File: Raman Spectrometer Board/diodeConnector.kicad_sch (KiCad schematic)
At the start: 15 parts, among them J5 Conn_01x02, Q1 BSS138, Q2 AO3401A, Q3 AO3401A, Q4 BSS138

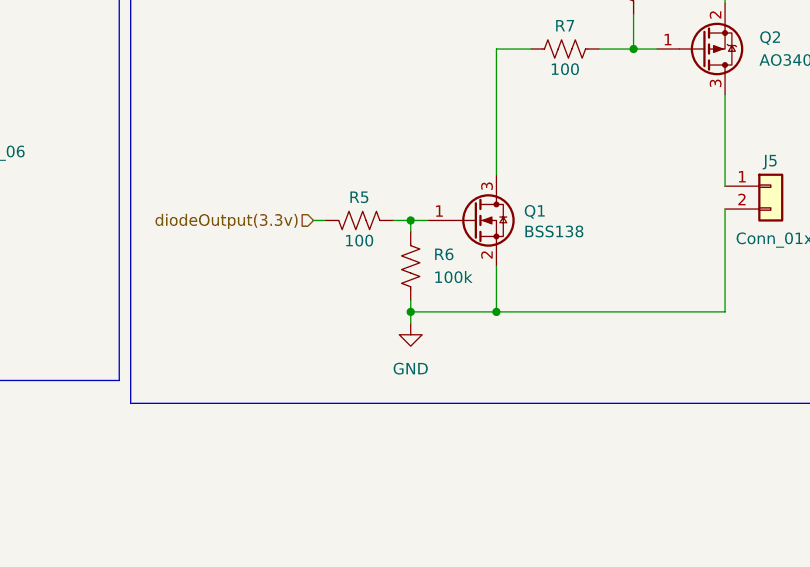
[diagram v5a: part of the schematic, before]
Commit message: Began re-laying out laser driver section
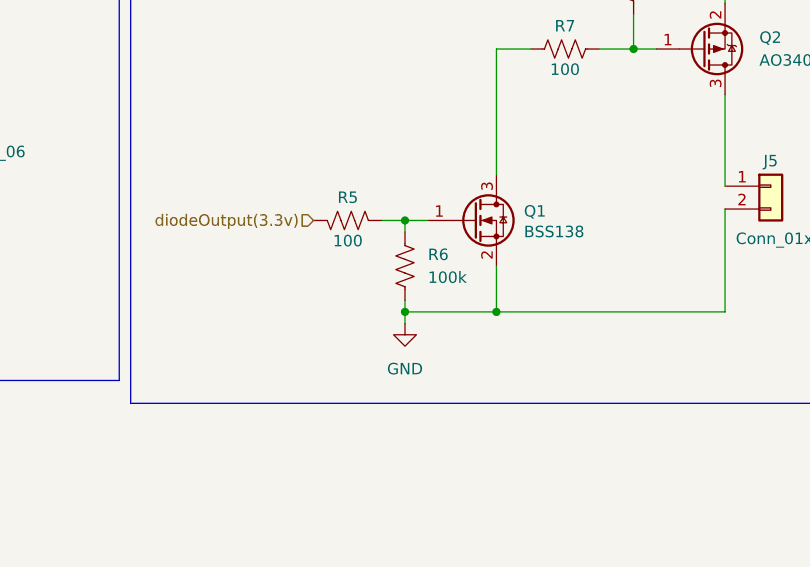
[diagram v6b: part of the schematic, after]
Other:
- moved on the sheet: R5, R6
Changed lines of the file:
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@@
 	)
 	(junction
-		(at 122.555 80.01)
+		(at 121.92 69.85)
 		(diameter 0)
 		(color 0 0 0 0)
@@
 	)
 	(junction
-		(at 236.22 34.29)
+		(at 121.92 80.01)
 		(diameter 0)
 		(color 0 0 0 0)
 	)
 	(junction
-		(at 122.555 69.85)
+		(at 236.22 34.29)
 		(diameter 0)
 		(color 0 0 0 0)
@@
 	(wire
 		(pts
+			(xy 121.92 69.85) (xy 119.38 69.85)
+		)
+		(stroke
+			(width 0)
+			(type default)
+		)
+	)
+	(wire
+		(pts
+			(xy 121.92 69.85) (xy 124.46 69.85)
+		)
+		(stroke
+			(width 0)
+			(type default)
+		)
+	)
+	(wire
+		(pts
 			(xy 252.73 73.66) (xy 261.62 73.66)
 		)
@@
 	(wire
 		(pts
-			(xy 122.555 78.74) (xy 122.555 80.01)
+			(xy 121.92 78.74) (xy 121.92 80.01)
 		)
 		(stroke
@@
 	(wire
 		(pts
-			(xy 122.555 80.01) (xy 132.08 80.01)
-		)
-		(stroke
-			(width 0)
-			(type default)
-		)
-	)
-	(wire
-		(pts
 			(xy 245.11 78.74) (xy 245.11 91.44)
 		)
@@
 	(wire
 		(pts
-			(xy 122.555 69.85) (xy 122.555 71.12)
-		)
-		(stroke
-			(width 0)
-			(type default)
-		)
-	)
-	(wire
-		(pts
-			(xy 124.46 69.85) (xy 122.555 69.85)
+			(xy 121.92 69.85) (xy 121.92 71.12)
 		)
 		(stroke
@@
 	(wire
 		(pts
+			(xy 121.92 80.01) (xy 132.08 80.01)
+		)
+		(stroke
+			(width 0)
+			(type default)
+		)
+	)
+	(wire
+		(pts
 			(xy 157.48 38.1) (xy 157.48 45.72)
 		)
@@
 	(wire
 		(pts
-			(xy 113.03 69.85) (xy 111.76 69.85)
-		)
-		(stroke
-			(width 0)
-			(type default)
-		)
-	)
-	(wire
-		(pts
 			(xy 157.48 36.83) (xy 157.48 38.1)
 		)
@@
 	(wire
 		(pts
-			(xy 122.555 80.01) (xy 122.555 81.28)
-		)
-		(stroke
-			(width 0)
-			(type default)
-		)
-	)
-	(wire
-		(pts
-			(xy 122.555 69.85) (xy 120.65 69.85)
+			(xy 121.92 80.01) (xy 121.92 81.28)
 		)
 		(stroke
@@
 		(dnp no)
 		(fields_autoplaced yes)
-		(property "Reference" "#PWR029"
+		(property "Reference" "#PWR032"
 			(at 228.6 97.79 0)
 			(effects
@@
 			(project "RamanSpectrometerBoard"
 				(path "/ab487c59-f066-48f5-a383-99e8eaf806bf/c790a08a-952a-47a5-8a2d-3628381b83e8"
-					(reference "#PWR029")
+					(reference "#PWR032")
 					(unit 1)
 				)
@@
 	(symbol
 		(lib_id "Device:R_US")
-		(at 122.555 74.93 180)
+		(at 121.92 74.93 180)
 		(unit 1)
 		(exclude_from_sim no)
@@
 		(dnp no)
 		(property "Reference" "R6"
-			(at 125.095 73.6599 0)
+			(at 124.46 73.6599 0)
 			(effects
 				(font
@@
 		)
 		(property "Value" "100k"
-			(at 125.095 76.1999 0)
+			(at 124.46 76.1999 0)
 			(effects
 				(font
@@
 		)
 		(property "Footprint" "Resistor_SMD:R_0603_1608Metric_Pad0.98x0.95mm_HandSolder"
-			(at 121.539 74.676 90)
+			(at 120.904 74.676 90)
 			(effects
 				(font
@@
 		)
 		(property "Datasheet" "~"
-			(at 122.555 74.93 0)
+			(at 121.92 74.93 0)
 			(effects
 				(font
@@
 		)
 		(property "Description" "Resistor, US symbol"
-			(at 122.555 74.93 0)
+			(at 121.92 74.93 0)
 			(effects
 				(font
@@
 		(dnp no)
 		(fields_autoplaced yes)
-		(property "Reference" "#PWR030"
+		(property "Reference" "#PWR033"
 			(at 236.22 35.56 0)
 			(effects
@@
 			(project ""
 				(path "/ab487c59-f066-48f5-a383-99e8eaf806bf/c790a08a-952a-47a5-8a2d-3628381b83e8"
-					(reference "#PWR030")
+					(reference "#PWR033")
 					(unit 1)
 				)
@@
 		(dnp no)
 		(fields_autoplaced yes)
-		(property "Reference" "#PWR023"
+		(property "Reference" "#PWR026"
 			(at 45.72 58.42 0)
 			(effects
@@
 			(project "RamanSpectrometerBoard"
 				(path "/ab487c59-f066-48f5-a383-99e8eaf806bf/c790a08a-952a-47a5-8a2d-3628381b83e8"
-					(reference "#PWR023")
+					(reference "#PWR026")
 					(unit 1)
 				)
@@
 		(dnp no)
 		(fields_autoplaced yes)
-		(property "Reference" "#PWR026"
+		(property "Reference" "#PWR029"
 			(at 58.42 153.67 0)
 			(effects
@@
 			(project "RamanSpectrometerBoard"
 				(path "/ab487c59-f066-48f5-a383-99e8eaf806bf/c790a08a-952a-47a5-8a2d-3628381b83e8"
-					(reference "#PWR026")
+					(reference "#PWR029")
 					(unit 1)
 				)
@@
 		(dnp no)
 		(fields_autoplaced yes)
-		(property "Reference" "#PWR025"
+		(property "Reference" "#PWR028"
 			(at 58.42 133.35 0)
 			(effects
@@
 			(project "RamanSpectrometerBoard"
 				(path "/ab487c59-f066-48f5-a383-99e8eaf806bf/c790a08a-952a-47a5-8a2d-3628381b83e8"
-					(reference "#PWR025")
+					(reference "#PWR028")
 					(unit 1)
 				)
@@
 	(symbol
 		(lib_id "Device:R_US")
-		(at 116.84 69.85 270)
+		(at 115.57 69.85 270)
 		(mirror x)
 		(unit 1)
@@
 		(dnp no)
 		(property "Reference" "R5"
-			(at 116.84 67.31 90)
+			(at 115.57 67.31 90)
 			(effects
 				(font
@@
 		)
 		(property "Value" "100"
-			(at 116.84 72.136 90)
+			(at 115.57 72.136 90)
 			(effects
 				(font
@@
 		)
 		(property "Footprint" "Resistor_SMD:R_0603_1608Metric_Pad0.98x0.95mm_HandSolder"
-			(at 116.586 68.834 90)
+			(at 115.316 68.834 90)
 			(effects
 				(font
@@
 		)
 		(property "Datasheet" "~"
-			(at 116.84 69.85 0)
+			(at 115.57 69.85 0)
 			(effects
 				(font
@@
 		)
 		(property "Description" "Resistor, US symbol"
-			(at 116.84 69.85 0)
+			(at 115.57 69.85 0)
 			(effects
 				(font
@@
 	(symbol
 		(lib_id "power:GND")
-		(at 122.555 81.28 0)
+		(at 121.92 81.28 0)
 		(mirror y)
 		(unit 1)
@@
 		(dnp no)
 		(fields_autoplaced yes)
-		(property "Reference" "#PWR027"
-			(at 122.555 87.63 0)
+		(property "Reference" "#PWR030"
+			(at 121.92 87.63 0)
 			(effects
 				(font
@@
 		)
 		(property "Value" "GND"
-			(at 122.555 86.36 0)
+			(at 121.92 86.36 0)
 			(effects
 				(font
@@
 		)
 		(property "Footprint" ""
-			(at 122.555 81.28 0)
+			(at 121.92 81.28 0)
 			(effects
 				(font
@@
 		)
 		(property "Datasheet" ""
-			(at 122.555 81.28 0)
+			(at 121.92 81.28 0)
 			(effects
 				(font
@@
 		)
 		(property "Description" "Power symbol creates a global label with name \"GND\" , ground"
-			(at 122.555 81.28 0)
+			(at 121.92 81.28 0)
 			(effects
 				(font
@@
 			(project "RamanSpectrometerBoard"
 				(path "/ab487c59-f066-48f5-a383-99e8eaf806bf/c790a08a-952a-47a5-8a2d-3628381b83e8"
-					(reference "#PWR027")
+					(reference "#PWR030")
 					(unit 1)
 				)
@@
 		(dnp no)
 		(fields_autoplaced yes)
-		(property "Reference" "#PWR024"
+		(property "Reference" "#PWR027"
 			(at 57.15 78.74 0)
 			(effects
@@
 			(project "RamanSpectrometerBoard"
 				(path "/ab487c59-f066-48f5-a383-99e8eaf806bf/c790a08a-952a-47a5-8a2d-3628381b83e8"
-					(reference "#PWR024")
+					(reference "#PWR027")
 					(unit 1)
 				)
@@
 		(dnp no)
 		(fields_autoplaced yes)
-		(property "Reference" "#PWR028"
+		(property "Reference" "#PWR031"
 			(at 157.48 40.64 0)
 			(effects
@@
 			(project ""
 				(path "/ab487c59-f066-48f5-a383-99e8eaf806bf/c790a08a-952a-47a5-8a2d-3628381b83e8"
-					(reference "#PWR028")
-					(unit 1)
-				)
+					(reference "#PWR031")
+					(unit 1)
+				)

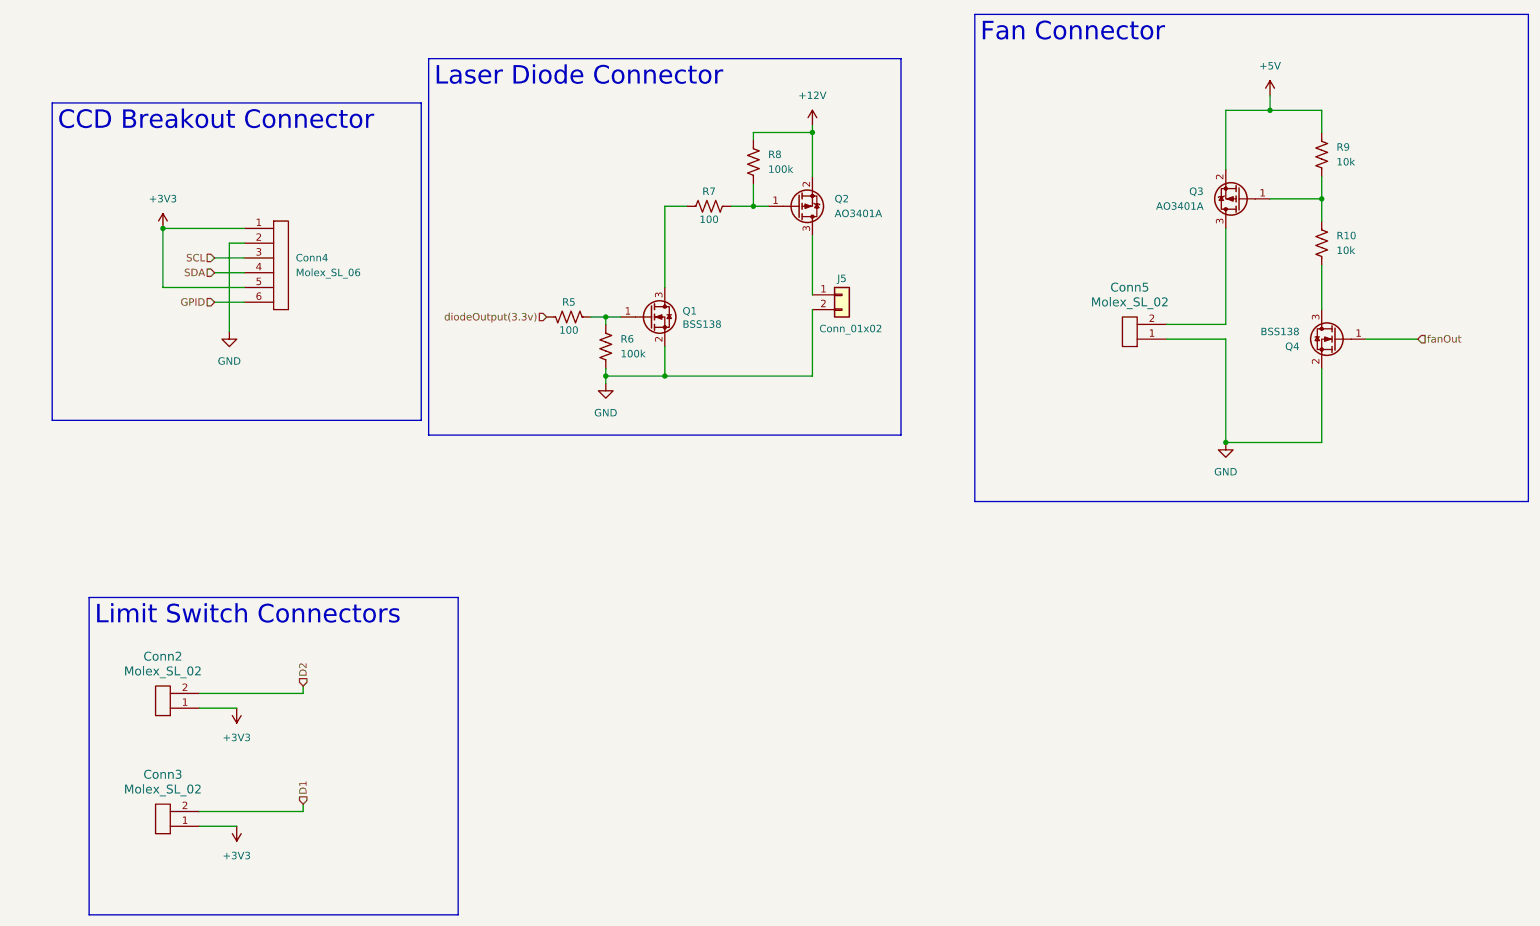
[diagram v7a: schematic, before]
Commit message: SCH fixes
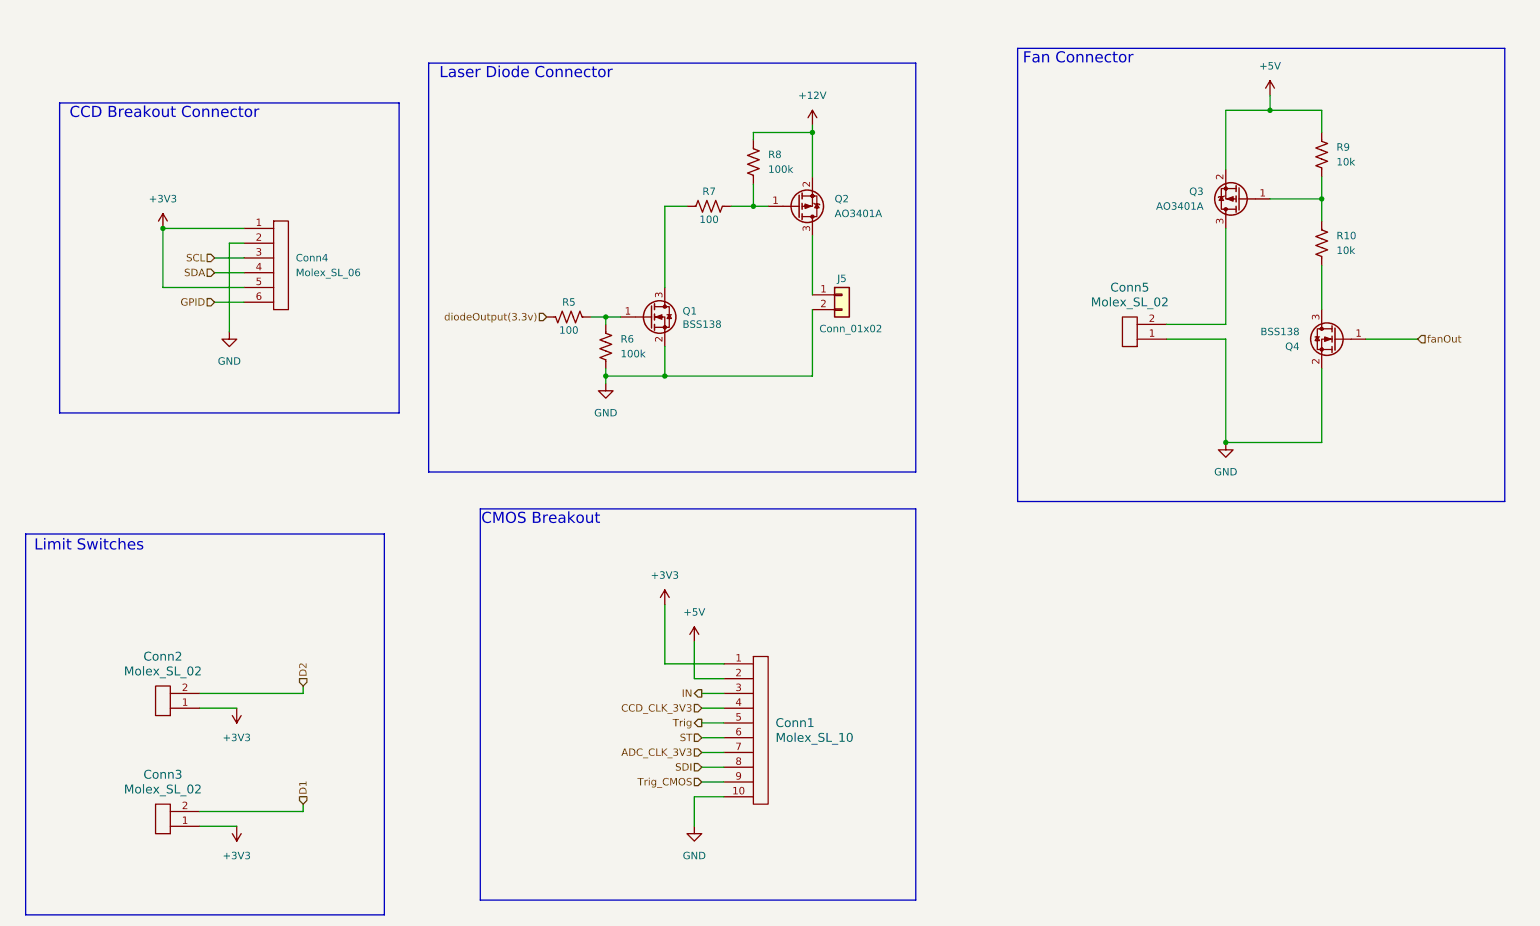
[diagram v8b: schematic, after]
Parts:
- added Conn1: Molex_SL_10, MRDT_Connectors:MOLEX_SL_10_Vertical, symbol MRDT_Connectors:Molex_SL_10
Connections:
- net +3V3: now also Conn1.1
- net +5V: now also Conn1.2
- net GND: now also Conn1.10
- new net ADC_CLK_3V3: Conn1.7
- new net CCD_CLK_3V3: Conn1.4
- new net IN: Conn1.3
- new net SDI: Conn1.8
- new net ST: Conn1.6
- new net Trig: Conn1.5
- new net Trig_CMOS: Conn1.9
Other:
- note added: "CCD Breakout Connector"
- note added: "CMOS Breakout"
- note added: "Fan Connector"
- note added: "Laser Diode Connector"
- note added: "Limit Switches"
